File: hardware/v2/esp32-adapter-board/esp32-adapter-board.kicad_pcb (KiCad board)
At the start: 2 copper layers, 80 x 30 mm, 6 parts

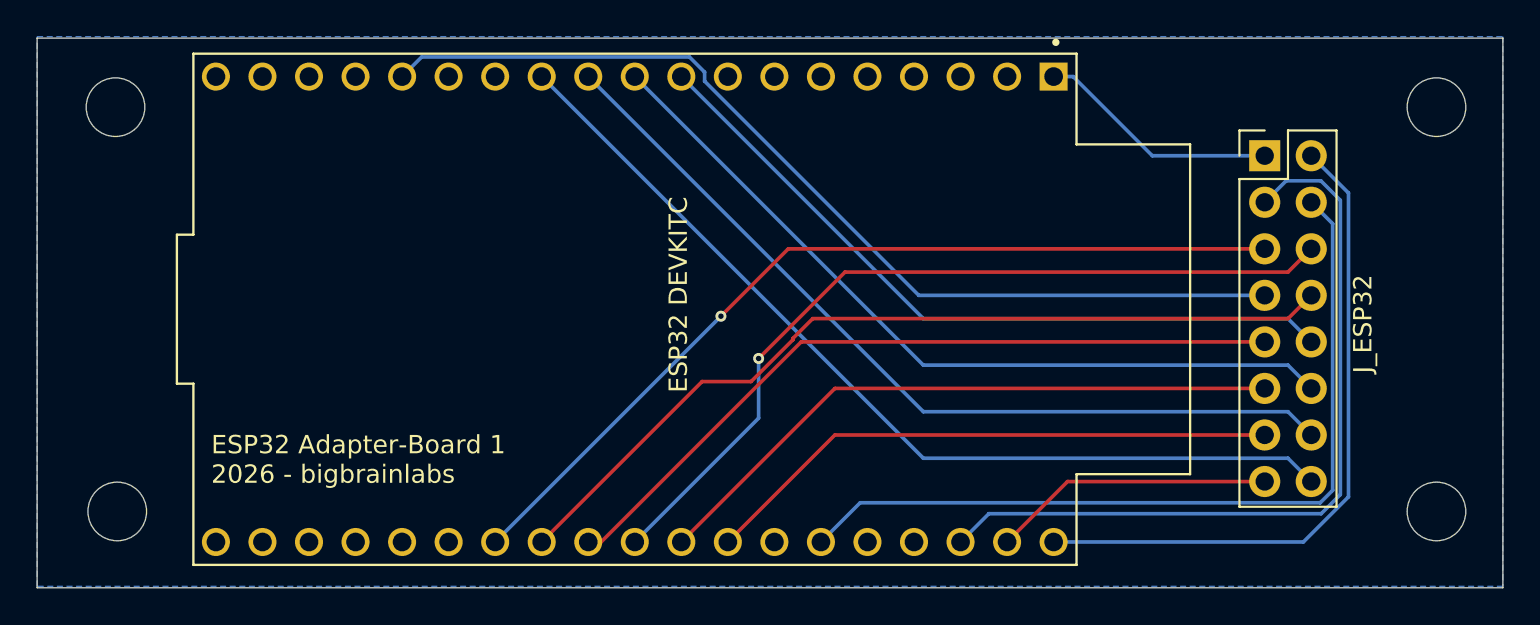
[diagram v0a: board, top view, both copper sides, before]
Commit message: Hardware v2: Input-Board neu generiert (Rev.1/Rev.2)
Gerber neu erzeugt, rev1/rev2-ZIP und Pick-&-Place-CSV ergänzt,
Schaltplan/Layout und Projektdateien aktualisiert.

Co-Authored-By: Claude Opus 4.8 <noreply@anthropic.com>
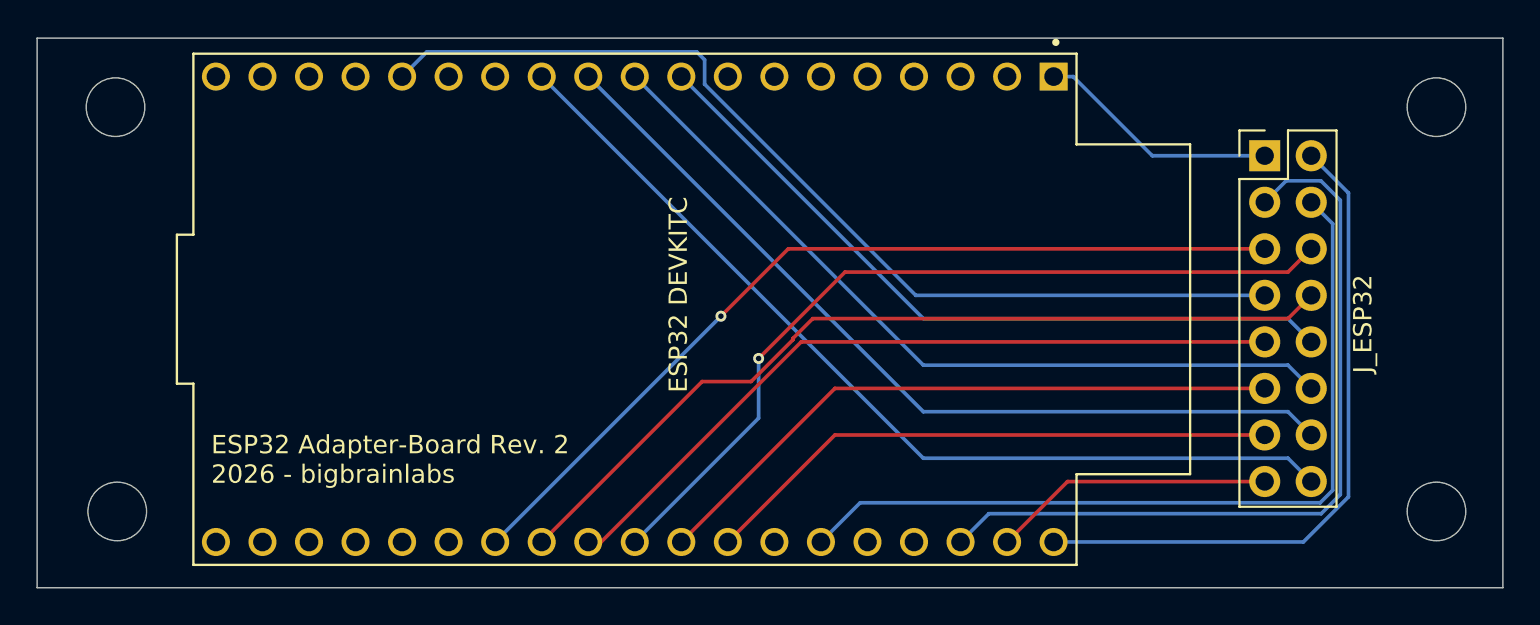
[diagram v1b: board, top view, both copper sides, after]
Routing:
- net Net-(J33-Pin_7): track 53.2 -> 53.9 mm
- removed copper zone on B.Cu, net GND
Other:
- board text added: "ESP32 Adapter-Board Rev. 2 2026 - bigbrainlabs"
- board text removed: "ESP32 Adapter-Board 1 2026 - bigbrainlabs"
